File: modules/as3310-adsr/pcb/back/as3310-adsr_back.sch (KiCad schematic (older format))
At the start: 22 parts, among them J1 IDC Header 2x8, J2 Pin Socket 1x9, U1 AS3310, U2 TL071

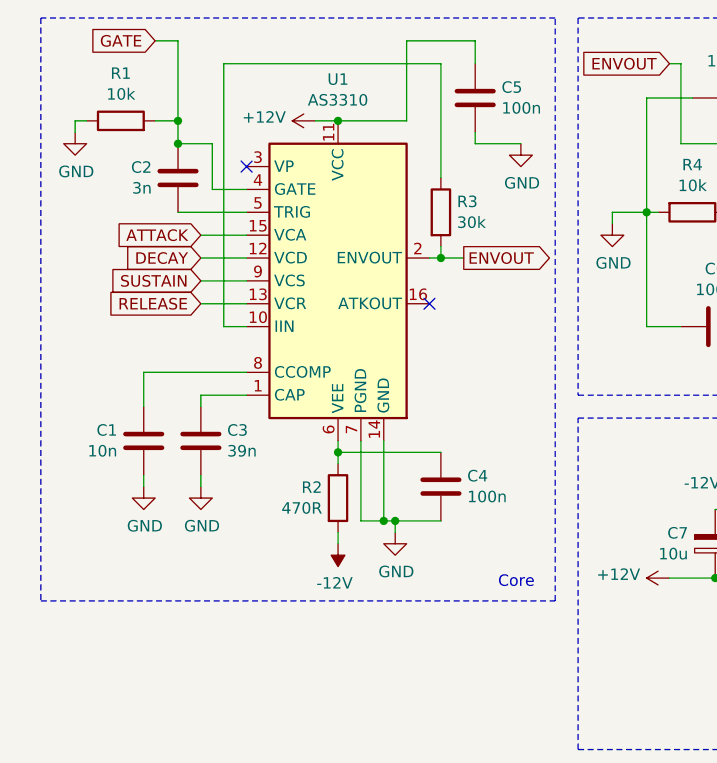
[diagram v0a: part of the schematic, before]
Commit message: modules: as3310-adsr: new revision for back pcb: 1.1
the module was missing a diode in the gate input to avoid burning the
AS3310 by applying negative voltage.

I fixed my boards by cutting and scrapping the gate track, close to R3
top pin and soldering an SMD version of 1N4148, like this:

https://filebin.xyz/UGnlaM44cwMN2fDaeGj87lC2
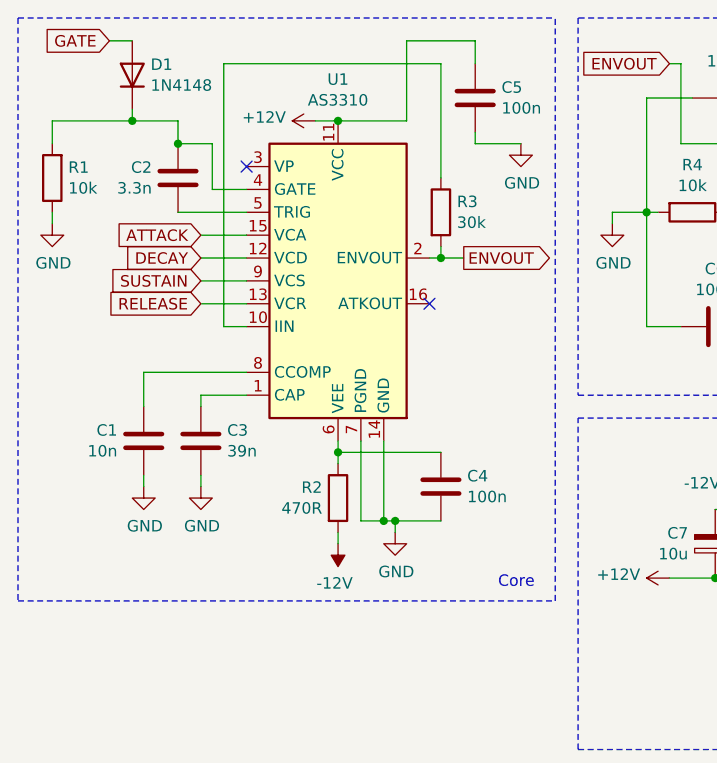
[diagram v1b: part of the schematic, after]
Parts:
- added D1: 1N4148, Diode_THT:D_DO-35_SOD27_P7.62mm_Horizontal, symbol Diode:1N4148
- C2: value 3n -> 3.3n
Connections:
- net GATE: now also D1.2 (A); no longer C2.1, R1.2, U1.4 (GATE)
- new net: C2.1, D1.1 (K), R1.2, U1.4 (GATE)
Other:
- moved on the sheet: R1
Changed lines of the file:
@@
 Title "as3310-adsr back"
 Date "2022-01-08"
-Rev "1.0"
+Rev "1.1"
 Comp ""
 Comment1 ""
@@
 P 3900 3050
 F 0 "C2" H 3786 3096 50  0000 R CNN
-F 1 "3n" H 3786 3005 50  0000 R CNN
+F 1 "3.3n" H 3786 3005 50  0000 R CNN
 F 2 "Capacitor_THT:C_Disc_D3.0mm_W1.6mm_P2.50mm" H 3938 2900 50  0001 C CNN
 F 3 "~" H 3900 3050 50  0001 C CNN
@@
 	4050 2900 3900 2900
 Wire Wire Line
-	3800 2800 3900 2800
-Wire Wire Line
 	3900 2800 3900 2900
 Connection ~ 3900 2900
@@
 L Device:R R1
 U 1 1 61DCBA6F
-P 3650 2800
-F 0 "R1" V 3857 2800 50  0000 C CNN
-F 1 "10k" V 3766 2800 50  0000 C CNN
-F 2 "Resistor_THT:R_Axial_DIN0207_L6.3mm_D2.5mm_P10.16mm_Horizontal" V 3580 2800 50  0001 C CNN
-F 3 "~" H 3650 2800 50  0001 C CNN
-	1    3650 2800
-	0    -1   -1   0
-$EndComp
-Wire Wire Line
-	3450 2800 3500 2800
+P 3350 3050
+F 0 "R1" H 3280 3004 50  0000 R CNN
+F 1 "10k" H 3280 3095 50  0000 R CNN
+F 2 "Resistor_THT:R_Axial_DIN0207_L6.3mm_D2.5mm_P10.16mm_Horizontal" V 3280 3050 50  0001 C CNN
+F 3 "~" H 3350 3050 50  0001 C CNN
+	1    3350 3050
+	-1   0    0    1
+$EndComp
 $Comp
 L power:GND #PWR01
 U 1 1 61DCF1B8
-P 3450 2850
-F 0 "#PWR01" H 3450 2600 50  0001 C CNN
-F 1 "GND" H 3455 2677 50  0000 C CNN
-F 2 "" H 3450 2850 50  0001 C CNN
-F 3 "" H 3450 2850 50  0001 C CNN
-	1    3450 2850
-	1    0    0    -1
-$EndComp
-Text GLabel 3800 2450 0    50   Input ~ 0
-GATE
-Wire Wire Line
-	3800 2450 3900 2450
-Wire Wire Line
-	3900 2450 3900 2800
-Connection ~ 3900 2800
-Wire Wire Line
-	3450 2850 3450 2800
+P 3350 3250
+F 0 "#PWR01" H 3350 3000 50  0001 C CNN
+F 1 "GND" H 3355 3077 50  0000 C CNN
+F 2 "" H 3350 3250 50  0001 C CNN
+F 3 "" H 3350 3250 50  0001 C CNN
+	1    3350 3250
+	1    0    0    -1
+$EndComp
 $Comp
 L Amplifier_Operational:TL071 U2
@@
 Wire Notes Line
 	5550 4900 5550 2350
-Wire Notes Line
-	5550 2350 3300 2350
-Wire Notes Line
-	3300 2350 3300 4900
-Wire Notes Line
-	3300 4900 5550 4900
 $Comp
 L Device:C C6
@@
 	1    0    0    -1
 $EndComp
+$Comp
+L Diode:1N4148 D1
+U 1 1 61E7DD23
+P 3700 2600
+F 0 "D1" V 3746 2520 50  0000 R CNN
+F 1 "1N4148" V 3655 2520 50  0000 R CNN
+F 2 "Diode_THT:D_DO-35_SOD27_P7.62mm_Horizontal" H 3700 2425 50  0001 C CNN
+F 3 "https://assets.nexperia.com/documents/data-sheet/1N4148_1N4448.pdf" H 3700 2600 50  0001 C CNN
+	1    3700 2600
+	0    -1   -1   0
+$EndComp
+Text GLabel 3600 2450 0    50   Input ~ 0
+GATE
+Wire Wire Line
+	3700 2750 3700 2800
+Connection ~ 3700 2800
+Wire Wire Line
+	3700 2800 3900 2800
+Wire Wire Line
+	3700 2450 3600 2450
+Wire Wire Line
+	3350 3250 3350 3200
+Wire Wire Line
+	3350 2900 3350 2800
+Wire Wire Line
+	3350 2800 3700 2800
+Wire Notes Line
+	3200 2350 3200 4900
+Wire Notes Line
+	3200 2350 5550 2350
+Wire Notes Line
+	3200 4900 5550 4900
 $EndSCHEMATC
